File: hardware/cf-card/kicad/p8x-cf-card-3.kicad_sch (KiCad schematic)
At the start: 3 parts, among them J1 MABC96R, J2 IDE-40 D0, J5 IDE-40 D1

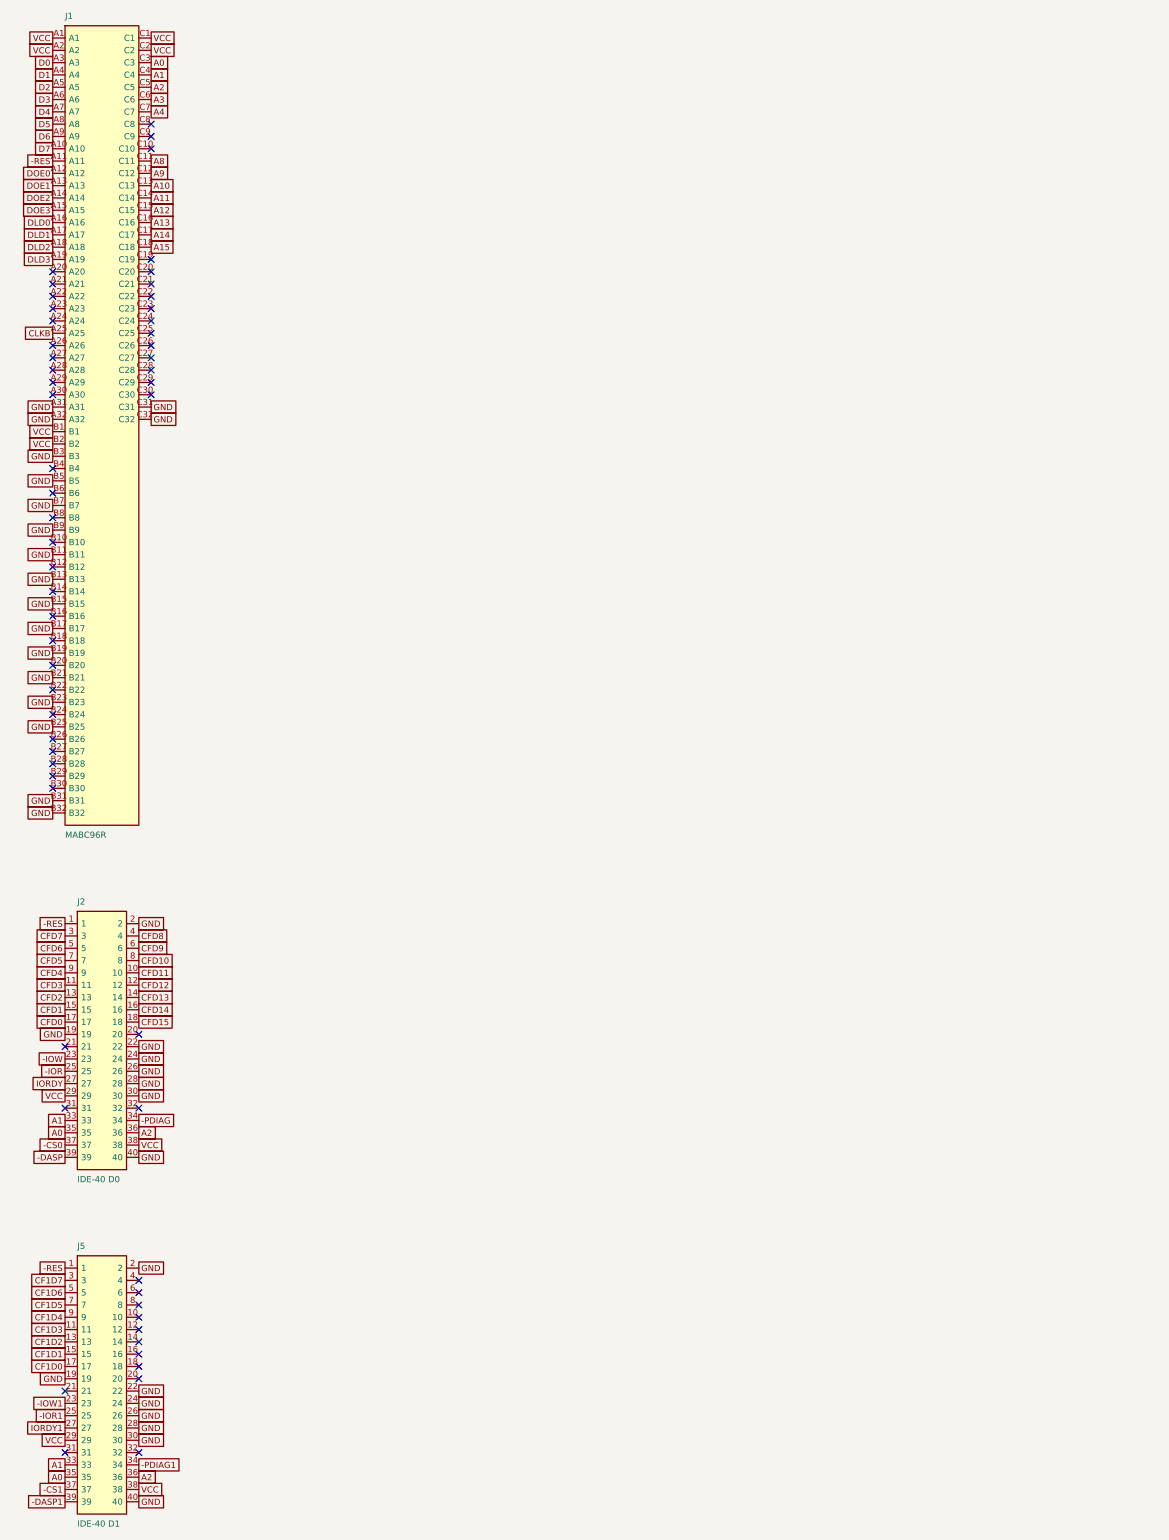
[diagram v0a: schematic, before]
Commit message: feat(sch): draw every P8X card schematic by function
Extend the functional-sheet grouping from the io-card to the control,
regbank, alu, memory, cf, ps2 and bustest cards. functional_sheets now
attaches unnamed glue gates, LEDs, resistors and connectors to the block
they share the most local nets with, so each block lists only its main
parts. A net with two or more pins on a sheet is now wired there even if
it continues elsewhere (its global name label rides on the wire), and
every wire is oriented by drawing side. The regbank gets one pointer per
sheet; the ps2 latches share a sheet with the AVR so the mailbox bus is
drawn. The bustest probe resistors use a straight-order RNISO8DSTR
drawing (the reversed B side forced every wire to cross and the sheet
fell back to labels). build_sch.sh now shows ELK fallbacks and clears old
numbered sheets before a build. All eight netlists match the boards,
ERC 0 errors; the boards change only in footprint link paths.

Co-Authored-By: Claude Opus 5.5 <noreply@anthropic.com>
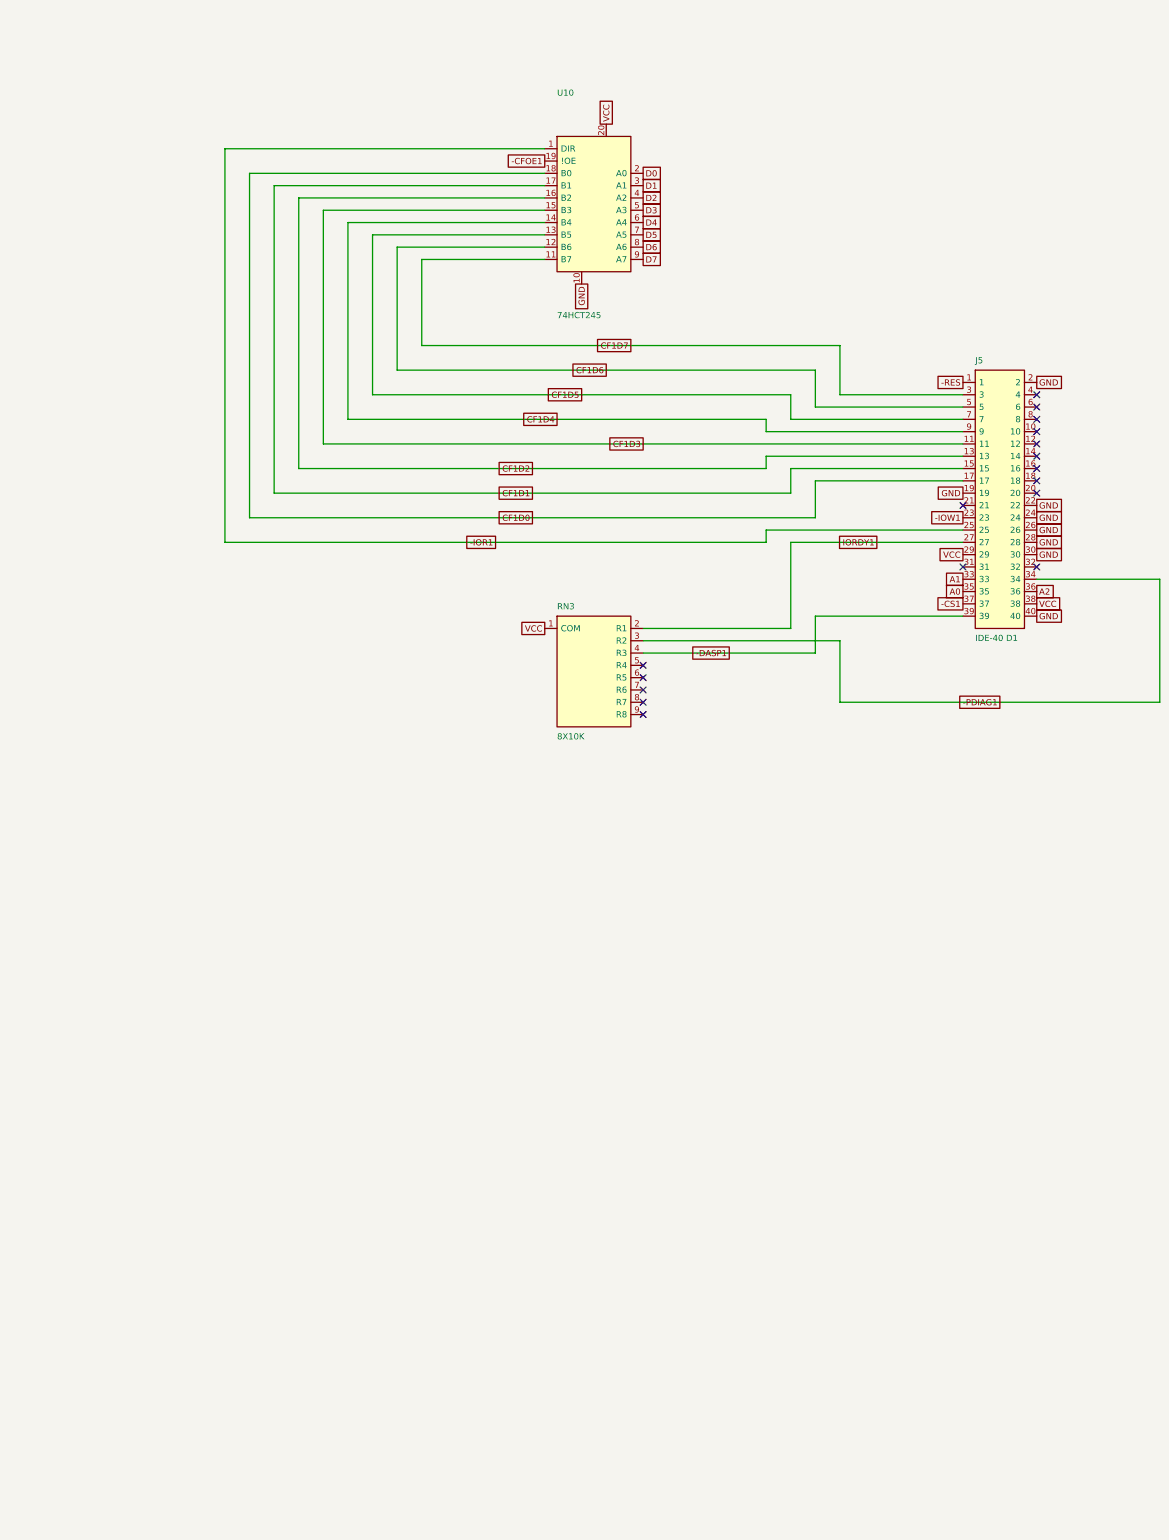
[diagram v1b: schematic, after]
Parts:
- removed J1: MABC96R, Connector_DIN:DIN41612_C_3x32_Male_Horizontal_THT, symbol p8x:DIN96C
- removed J2: IDE-40 D0, Connector_IDC:IDC-Header_2x20_P2.54mm_Vertical, symbol p8x:IDE40
- added RN3: 8X10K, Resistor_THT:R_Array_SIP9, symbol p8x:SIP9
- added U10: 74HCT245, Package_DIP:DIP-20_W7.62mm, symbol p8x:74245
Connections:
- net -DASP1: now also RN3.4 (R3)
- net -IOR1: now also U10.1 (DIR)
- net -PDIAG1: now also RN3.3 (R2)
- net CF1D0: now also U10.18 (B0)
- net CF1D1: now also U10.17 (B1)
- net CF1D2: now also U10.16 (B2)
- net CF1D3: now also U10.15 (B3)
- net CF1D4: now also U10.14 (B4)
- net CF1D5: now also U10.13 (B5)
- net CF1D6: now also U10.12 (B6)
- net CF1D7: now also U10.11 (B7)
- net D0: now also U10.2 (A0)
- net D1: now also U10.3 (A1)
- net D2: now also U10.4 (A2)
- net D3: now also U10.5 (A3)
- net D4: now also U10.6 (A4)
- net D5: now also U10.7 (A5)
- net D6: now also U10.8 (A6)
- net D7: now also U10.9 (A7)
- net GND: now also U10.10
- net IORDY1: now also RN3.2 (R1)
- net VCC: now also RN3.1 (COM), U10.20
- new net -CFOE1: U10.19 (!OE)
- no-connect marks 57 -> 17
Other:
- moved on the sheet: J5
